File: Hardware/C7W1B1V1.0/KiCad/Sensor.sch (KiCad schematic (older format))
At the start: 10 parts, among them J2 PMS3003, U2 BME688

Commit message: Dodano projekt Cube
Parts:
- renumbered J2 to J1, R4 to R3, R5 to R4, R6 to R5, R7 to R6, R8 to R7
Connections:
- net GND: now also J1.3 (Pin_3); no longer J1.8 (Pin_8)
- net PMS_RST: now also J1.4 (Pin_4); no longer J1.6 (Pin_6)
- net PMS_TX: now also J1.8 (Pin_8); no longer J1.3 (Pin_3)
- net PMS_SET: now reaches J1.2 (Pin_2), R7.2
- new net PMS_RX: J1.6 (Pin_6)
- no-connect marks 3 -> 2
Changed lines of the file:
@@
 P 3900 1450
 AR Path="/672E4D00/673033A4" Ref="R?"  Part="1"
-AR Path="/672E4DB0/673033A4" Ref="R5"  Part="1"
-F 0 "R5" H 3970 1496 50  0000 L CNN
+AR Path="/672E4DB0/673033A4" Ref="R4"  Part="1"
+F 0 "R4" H 3970 1496 50  0000 L CNN
 F 1 "10k/5%/0.063W" V 3800 1150 50  0000 L CNN
 F 2 "Resistor_SMD:R_0402_1005Metric" V 3830 1450 50  0001 C CNN
@@
 $EndComp
 $Comp
-L power:GND #PWR0110
+L power:GND #PWR015
 U 1 1 673034DE
 P 4950 2400
-F 0 "#PWR0110" H 4950 2150 50  0001 C CNN
+F 0 "#PWR015" H 4950 2150 50  0001 C CNN
 F 1 "GND" H 4955 2227 50  0000 C CNN
 F 2 "" H 4950 2400 50  0001 C CNN
@@
 $EndComp
 $Comp
-L power:+3V3 #PWR0111
+L power:+3V3 #PWR012
 U 1 1 673036AD
 P 3900 1150
-F 0 "#PWR0111" H 3900 1000 50  0001 C CNN
+F 0 "#PWR012" H 3900 1000 50  0001 C CNN
 F 1 "+3V3" H 3915 1323 50  0000 C CNN
 F 2 "" H 3900 1150 50  0001 C CNN
@@
 P 4250 1450
 AR Path="/672E4D00/673050A1" Ref="R?"  Part="1"
-AR Path="/672E4DB0/673050A1" Ref="R6"  Part="1"
-F 0 "R6" H 4320 1496 50  0000 L CNN
+AR Path="/672E4DB0/673050A1" Ref="R5"  Part="1"
+F 0 "R5" H 4320 1496 50  0000 L CNN
 F 1 "10k/5%/0.063W" V 4150 1150 50  0000 L CNN
 F 2 "Resistor_SMD:R_0402_1005Metric" V 4180 1450 50  0001 C CNN
@@
 P 4600 1450
 AR Path="/672E4D00/673054D4" Ref="R?"  Part="1"
-AR Path="/672E4DB0/673054D4" Ref="R7"  Part="1"
-F 0 "R7" H 4670 1496 50  0000 L CNN
+AR Path="/672E4DB0/673054D4" Ref="R6"  Part="1"
+F 0 "R6" H 4670 1496 50  0000 L CNN
 F 1 "10k/5%/0.063W" V 4500 1150 50  0000 L CNN
 F 2 "Resistor_SMD:R_0402_1005Metric" V 4530 1450 50  0001 C CNN
@@
 P 2350 2550
 AR Path="/672E4D00/67306106" Ref="R?"  Part="1"
-AR Path="/672E4DB0/67306106" Ref="R4"  Part="1"
-F 0 "R4" H 2420 2596 50  0000 L CNN
+AR Path="/672E4DB0/67306106" Ref="R3"  Part="1"
+F 0 "R3" H 2420 2596 50  0000 L CNN
 F 1 "10k/5%/0.063W" V 2250 2250 50  0000 L CNN
 F 2 "Resistor_SMD:R_0402_1005Metric" V 2280 2550 50  0001 C CNN
@@
 $EndComp
 $Comp
-L power:GND #PWR0112
+L power:GND #PWR011
 U 1 1 67306692
 P 2350 2800
-F 0 "#PWR0112" H 2350 2550 50  0001 C CNN
+F 0 "#PWR011" H 2350 2550 50  0001 C CNN
 F 1 "GND" H 2355 2627 50  0000 C CNN
 F 2 "" H 2350 2800 50  0001 C CNN
@@
 	2350 2700 2350 2800
 $Comp
-L power:+3V3 #PWR0113
+L power:+3V3 #PWR013
 U 1 1 67306A3C
 P 4250 1150
-F 0 "#PWR0113" H 4250 1000 50  0001 C CNN
+F 0 "#PWR013" H 4250 1000 50  0001 C CNN
 F 1 "+3V3" H 4265 1323 50  0000 C CNN
 F 2 "" H 4250 1150 50  0001 C CNN
@@
 	4250 1150 4250 1300
 $Comp
-L power:+3V3 #PWR0114
+L power:+3V3 #PWR014
 U 1 1 67306EA3
 P 4600 1150
-F 0 "#PWR0114" H 4600 1000 50  0001 C CNN
+F 0 "#PWR014" H 4600 1000 50  0001 C CNN
 F 1 "+3V3" H 4615 1323 50  0000 C CNN
 F 2 "" H 4600 1150 50  0001 C CNN
@@
 Connection ~ 2100 1750
 $Comp
-L power:+3V3 #PWR0115
+L power:+3V3 #PWR09
 U 1 1 67308A5B
 P 2100 1600
-F 0 "#PWR0115" H 2100 1450 50  0001 C CNN
+F 0 "#PWR09" H 2100 1450 50  0001 C CNN
 F 1 "+3V3" H 2115 1773 50  0000 C CNN
 F 2 "" H 2100 1600 50  0001 C CNN
@@
 $EndComp
 $Comp
-L power:GND #PWR0116
+L power:GND #PWR010
 U 1 1 673090AA
 P 2100 2100
-F 0 "#PWR0116" H 2100 1850 50  0001 C CNN
+F 0 "#PWR010" H 2100 1850 50  0001 C CNN
 F 1 "GND" H 2105 1927 50  0000 C CNN
 F 2 "" H 2100 2100 50  0001 C CNN
@@
 	2200 2350 1500 2350
 $Comp
-L power:GND #PWR0117
+L power:GND #PWR08
 U 1 1 6730B0F7
 P 1500 2650
-F 0 "#PWR0117" H 1500 2400 50  0001 C CNN
+F 0 "#PWR08" H 1500 2400 50  0001 C CNN
 F 1 "GND" H 1505 2477 50  0000 C CNN
 F 2 "" H 1500 2650 50  0001 C CNN
@@
 Connection ~ 1500 2350
 $Comp
-L power:+3V3 #PWR0118
+L power:+3V3 #PWR07
 U 1 1 6730CB2F
 P 1500 2200
-F 0 "#PWR0118" H 1500 2050 50  0001 C CNN
+F 0 "#PWR07" H 1500 2050 50  0001 C CNN
 F 1 "+3V3" H 1515 2373 50  0000 C CNN
 F 2 "" H 1500 2200 50  0001 C CNN
@@
 P 6300 4000
 AR Path="/672EED17/6730E0F9" Ref="J?"  Part="1"
-AR Path="/672E4DB0/6730E0F9" Ref="J2"  Part="1"
-F 0 "J2" H 6350 4317 50  0000 C CNN
+AR Path="/672E4DB0/6730E0F9" Ref="J1"  Part="1"
+F 0 "J1" H 6350 4317 50  0000 C CNN
 F 1 "PMS3003" H 6350 4226 50  0000 C CNN
 F 2 "Connector_PinHeader_2.54mm:PinHeader_2x04_P2.54mm_Vertical" H 6300 4000 50  0001 C CNN
@@
 $EndComp
 Wire Wire Line
-	6600 3900 6750 3900
-Wire Wire Line
-	6750 3900 6750 3300
-Wire Wire Line
 	6100 3900 5950 3900
 Wire Wire Line
@@
 	5950 3150 5950 3300
 $Comp
-L power:GND #PWR0119
+L power:GND #PWR017
 U 1 1 6731A3A3
 P 6600 3300
-F 0 "#PWR0119" H 6600 3050 50  0001 C CNN
+F 0 "#PWR017" H 6600 3050 50  0001 C CNN
 F 1 "GND" H 6605 3127 50  0000 C CNN
 F 2 "" H 6600 3300 50  0001 C CNN
@@
 $EndComp
 Wire Wire Line
-	6750 3300 6600 3300
-Connection ~ 6600 3300
-Wire Wire Line
 	6600 3300 6500 3300
 $Comp
-L power:+5V #PWR0120
+L power:+5V #PWR016
 U 1 1 6731C33D
 P 5950 3150
-F 0 "#PWR0120" H 5950 3000 50  0001 C CNN
+F 0 "#PWR016" H 5950 3000 50  0001 C CNN
 F 1 "+5V" H 5965 3323 50  0000 C CNN
 F 2 "" H 5950 3150 50  0001 C CNN
@@
 P 5750 3500
 AR Path="/672E4D00/6731DBE5" Ref="R?"  Part="1"
-AR Path="/672E4DB0/6731DBE5" Ref="R8"  Part="1"
-F 0 "R8" V 5850 3450 50  0000 L CNN
+AR Path="/672E4DB0/6731DBE5" Ref="R7"  Part="1"
+F 0 "R7" V 5850 3450 50  0000 L CNN
 F 1 "10k/5%/0.063W" V 5650 3200 50  0000 L CNN
 F 2 "Resistor_SMD:R_0402_1005Metric" V 5680 3500 50  0001 C CNN
@@
 Connection ~ 5950 3300
 NoConn ~ 6600 4000
-Text GLabel 6100 4100 0    50   Output ~ 0
+Text GLabel 6600 3900 2    50   Output ~ 0
 PMS_TX
+Text GLabel 6100 4200 0    50   Input ~ 0
+PMS_RST
+NoConn ~ 6600 4200
 Text GLabel 6600 4100 2    50   Input ~ 0
-PMS_RST
-NoConn ~ 6100 4200
-NoConn ~ 6600 4200
+PMS_RX
+Text GLabel 5750 4000 0    50   Input ~ 0
+PMS_SET
+$Comp
+L power:GND #PWR0101
+U 1 1 673DEE2F
+P 5400 4200
+F 0 "#PWR0101" H 5400 3950 50  0001 C CNN
+F 1 "GND" H 5405 4027 50  0000 C CNN
+F 2 "" H 5400 4200 50  0001 C CNN
+F 3 "" H 5400 4200 50  0001 C CNN
+	1    5400 4200
+	1    0    0    -1
+$EndComp
+Wire Wire Line
+	6100 4100 5400 4100
+Wire Wire Line
+	5400 4100 5400 4200
 $EndSCHEMATC

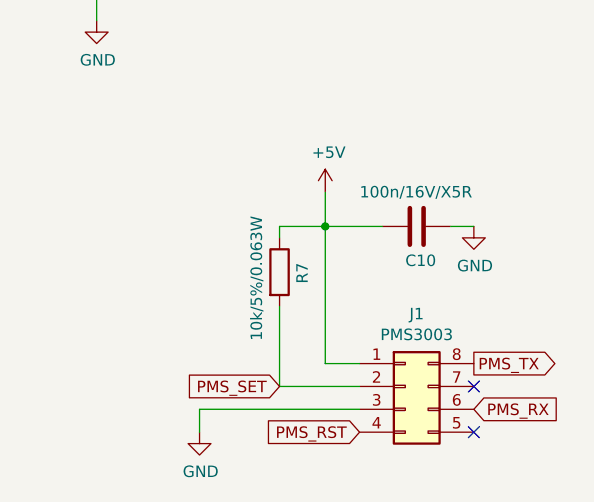
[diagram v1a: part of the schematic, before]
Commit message: Ukończono PCB. dodano pliki produkcyjne
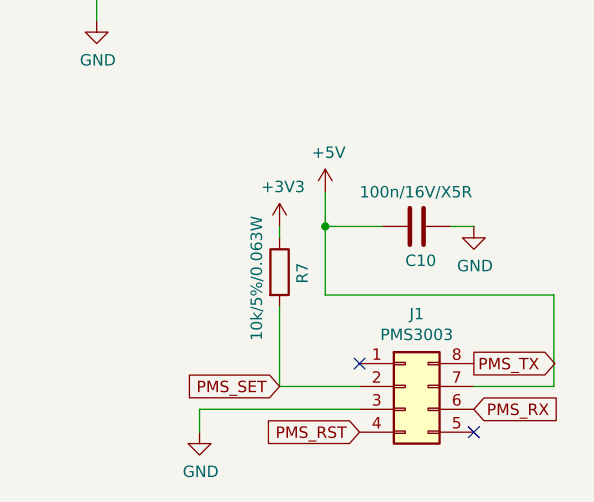
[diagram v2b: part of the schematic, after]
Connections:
- net +3V3: now also R7.1
- net +5V: now also J1.7 (Pin_7); no longer J1.1 (Pin_1), R7.1
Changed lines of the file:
@@
 $EndComp
 Wire Wire Line
-	6100 3900 5950 3900
-Wire Wire Line
-	5950 3900 5950 3300
+	6950 4000 6950 3600
 Wire Wire Line
 	5950 3300 6200 3300
@@
 	5950 3150 5950 3300
 $Comp
-L power:GND #PWR017
+L power:GND #PWR018
 U 1 1 6731A3A3
 P 6600 3300
-F 0 "#PWR017" H 6600 3050 50  0001 C CNN
+F 0 "#PWR018" H 6600 3050 50  0001 C CNN
 F 1 "GND" H 6605 3127 50  0000 C CNN
 F 2 "" H 6600 3300 50  0001 C CNN
@@
 	6600 3300 6500 3300
 $Comp
-L power:+5V #PWR016
+L power:+5V #PWR017
 U 1 1 6731C33D
 P 5950 3150
-F 0 "#PWR016" H 5950 3000 50  0001 C CNN
+F 0 "#PWR017" H 5950 3000 50  0001 C CNN
 F 1 "+5V" H 5965 3323 50  0000 C CNN
 F 2 "" H 5950 3150 50  0001 C CNN
@@
 Wire Wire Line
 	5750 3350 5750 3300
-Wire Wire Line
-	5750 3300 5950 3300
 Connection ~ 5950 3300
-NoConn ~ 6600 4000
 Text GLabel 6600 3900 2    50   Output ~ 0
 PMS_TX
@@
 PMS_SET
 $Comp
-L power:GND #PWR0101
+L power:GND #PWR016
 U 1 1 673DEE2F
 P 5400 4200
-F 0 "#PWR0101" H 5400 3950 50  0001 C CNN
+F 0 "#PWR016" H 5400 3950 50  0001 C CNN
 F 1 "GND" H 5405 4027 50  0000 C CNN
 F 2 "" H 5400 4200 50  0001 C CNN
@@
 Wire Wire Line
 	5400 4100 5400 4200
+Wire Wire Line
+	6600 4000 6950 4000
+Wire Wire Line
+	6950 3600 5950 3600
+Wire Wire Line
+	5950 3600 5950 3300
+NoConn ~ 6100 3900
+$Comp
+L power:+3V3 #PWR0107
+U 1 1 675334F0
+P 5750 3300
+F 0 "#PWR0107" H 5750 3150 50  0001 C CNN
+F 1 "+3V3" H 5765 3473 50  0000 C CNN
+F 2 "" H 5750 3300 50  0001 C CNN
+F 3 "" H 5750 3300 50  0001 C CNN
+	1    5750 3300
+	1    0    0    -1
+$EndComp
 $EndSCHEMATC
